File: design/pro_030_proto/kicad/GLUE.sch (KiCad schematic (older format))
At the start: 14 parts, among them IC13 74HCT174, X2 8MHz

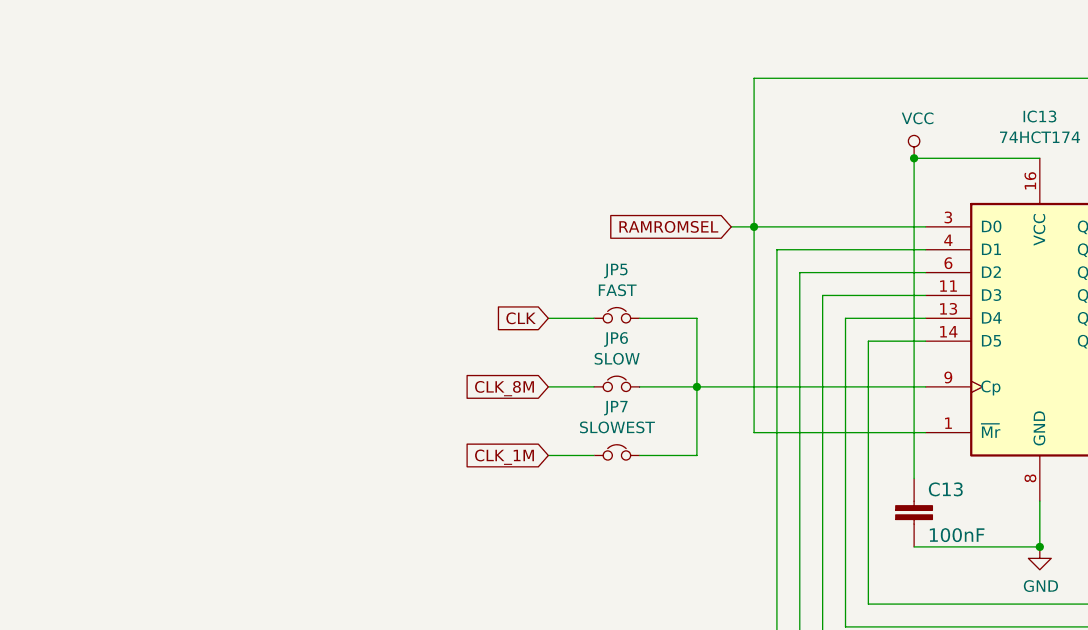
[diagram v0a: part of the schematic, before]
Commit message: Add new Xosera DTACK stretch GAL
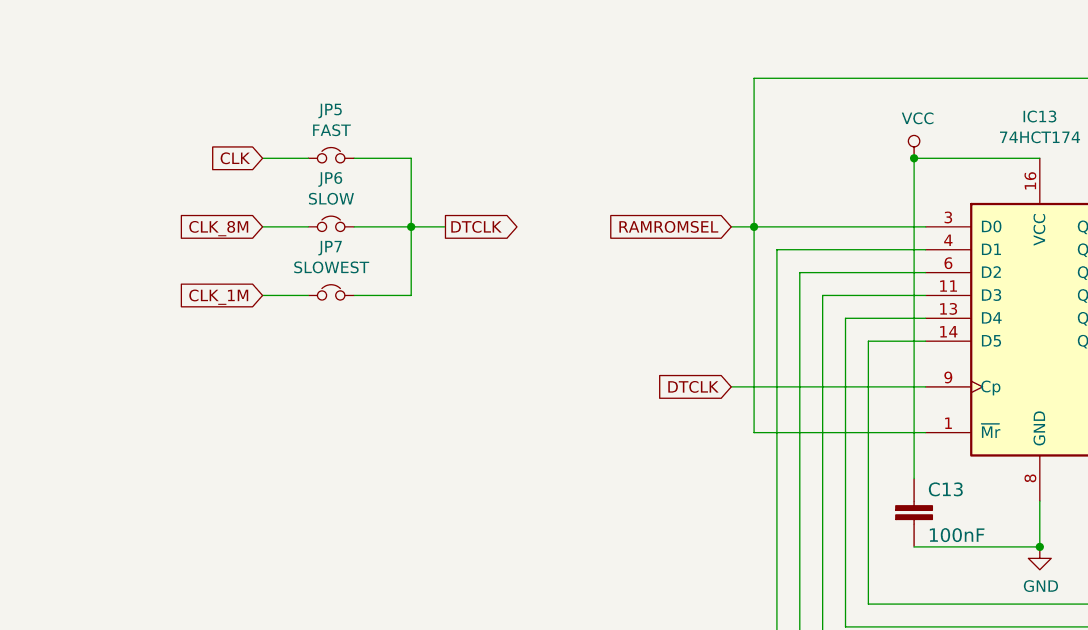
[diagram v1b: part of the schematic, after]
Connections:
- net DTCLK: now reaches IC13.9 (Cp), JP5.2, JP6.2, JP7.2
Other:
- moved on the sheet: JP5, JP6, JP7
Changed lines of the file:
@@
 Wire Wire Line
 	6850 3000 7500 3000
-Text GLabel 5850 3300 0    50   Input ~ 0
+Text GLabel 4600 2600 0    50   Input ~ 0
 CLK
 Wire Wire Line
@@
 L Device:Jumper_NC_Small JP5
 U 1 1 60FDCB26
-P 6150 3300
-F 0 "JP5" H 6150 3512 50  0000 C CNN
-F 1 "FAST" H 6150 3421 50  0000 C CNN
-F 2 "Connector_PinHeader_2.54mm:PinHeader_1x02_P2.54mm_Vertical" H 6150 3300 50  0001 C CNN
-F 3 "~" H 6150 3300 50  0001 C CNN
-	1    6150 3300
+P 4900 2600
+F 0 "JP5" H 4900 2812 50  0000 C CNN
+F 1 "FAST" H 4900 2721 50  0000 C CNN
+F 2 "Connector_PinHeader_2.54mm:PinHeader_1x02_P2.54mm_Vertical" H 4900 2600 50  0001 C CNN
+F 3 "~" H 4900 2600 50  0001 C CNN
+	1    4900 2600
 	1    0    0    -1
 $EndComp
@@
 L Device:Jumper_NC_Small JP6
 U 1 1 60FE19EE
-P 6150 3600
-F 0 "JP6" H 6150 3812 50  0000 C CNN
-F 1 "SLOW" H 6150 3721 50  0000 C CNN
-F 2 "Connector_PinHeader_2.54mm:PinHeader_1x02_P2.54mm_Vertical" H 6150 3600 50  0001 C CNN
-F 3 "~" H 6150 3600 50  0001 C CNN
-	1    6150 3600
+P 4900 2900
+F 0 "JP6" H 4900 3112 50  0000 C CNN
+F 1 "SLOW" H 4900 3021 50  0000 C CNN
+F 2 "Connector_PinHeader_2.54mm:PinHeader_1x02_P2.54mm_Vertical" H 4900 2900 50  0001 C CNN
+F 3 "~" H 4900 2900 50  0001 C CNN
+	1    4900 2900
 	1    0    0    -1
 $EndComp
@@
 L Device:Jumper_NC_Small JP7
 U 1 1 60FE6839
-P 6150 3900
-F 0 "JP7" H 6150 4112 50  0000 C CNN
-F 1 "SLOWEST" H 6150 4021 50  0000 C CNN
-F 2 "Connector_PinHeader_2.54mm:PinHeader_1x02_P2.54mm_Vertical" H 6150 3900 50  0001 C CNN
-F 3 "~" H 6150 3900 50  0001 C CNN
-	1    6150 3900
-	1    0    0    -1
-$EndComp
-Text GLabel 5850 3900 0    50   Input ~ 0
+P 4900 3200
+F 0 "JP7" H 4900 3412 50  0000 C CNN
+F 1 "SLOWEST" H 4900 3321 50  0000 C CNN
+F 2 "Connector_PinHeader_2.54mm:PinHeader_1x02_P2.54mm_Vertical" H 4900 3200 50  0001 C CNN
+F 3 "~" H 4900 3200 50  0001 C CNN
+	1    4900 3200
+	1    0    0    -1
+$EndComp
+Text GLabel 4600 3200 0    50   Input ~ 0
 CLK_1M
-Text GLabel 5850 3600 0    50   Input ~ 0
+Text GLabel 4600 2900 0    50   Input ~ 0
 CLK_8M
 Wire Wire Line
-	5850 3300 6050 3300
-Wire Wire Line
-	5850 3600 6050 3600
-Wire Wire Line
-	5850 3900 6050 3900
-Wire Wire Line
-	6250 3600 6500 3600
-Wire Wire Line
-	6250 3300 6500 3300
-Wire Wire Line
-	6500 3300 6500 3600
-Connection ~ 6500 3600
-Wire Wire Line
-	6500 3600 7500 3600
-Wire Wire Line
-	6500 3900 6500 3600
-Wire Wire Line
-	6250 3900 6500 3900
+	4600 2600 4800 2600
+Wire Wire Line
+	4600 2900 4800 2900
+Wire Wire Line
+	4600 3200 4800 3200
+Wire Wire Line
+	5000 2900 5250 2900
+Wire Wire Line
+	5000 2600 5250 2600
+Wire Wire Line
+	5250 2600 5250 2900
+Connection ~ 5250 2900
+Wire Wire Line
+	5250 3200 5250 2900
+Wire Wire Line
+	5000 3200 5250 3200
 Text GLabel 2900 3500 2    50   Output ~ 0
 CLK_8M
@@
 	0    -1   -1   0
 $EndComp
+Text GLabel 5400 2900 2    50   Output ~ 0
+DTCLK
+Wire Wire Line
+	5250 2900 5400 2900
+Text GLabel 6650 3600 0    50   Input ~ 0
+DTCLK
+Wire Wire Line
+	6650 3600 7500 3600
 $EndSCHEMATC
